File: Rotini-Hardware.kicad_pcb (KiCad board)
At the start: 4 copper layers, 62 x 21.6 mm, 116 parts, among them J1 Conn_01x02, J2 Conn_01x02, J200 SH_PPM, J201 SH_LED, J202 SH_LED, J60 Conn_Coaxial, Q20 AO3401A, Q30 LBSS84LT1G, Q31 2N7002, Q32 LBSS84LT1G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

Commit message: Hardware bought of Rotini V2
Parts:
- removed C50, C51: 100nF, Capacitor_SMD:C_0402_1005Metric
- removed C52: 10uF, Capacitor_SMD:C_0402_1005Metric
- removed J1, J2: Conn_01x02, Connector_PinHeader_2.54mm:PinHeader_1x02_P2.54mm_Vertical
- removed J200: SH_PPM, Connector_JST:JST_SH_SM04B-SRSS-TB_1x04-1MP_P1.00mm_Horizontal
- removed Q50, Q51: SS8050, Package_TO_SOT_SMD:SOT-23
- removed R10, R6, R7, R8, R9: 300R, Resistor_SMD:R_1206_3216Metric
- removed R2: 500R, Resistor_SMD:R_0402_1005Metric
- removed R50, R51, R52, R53: 1K, Resistor_SMD:R_0402_1005Metric
- removed R54, R55: 5.1K, Resistor_SMD:R_0402_1005Metric
- removed U50: CP2102-GMR, Package_DFN_QFN:QFN-28-1EP_5x5mm_P0.5mm_EP3.35x3.35mm
- removed U51: USB_C_Receptacle, AlfredoFootprints:USB_TYPE-C-31-M-12
- added ?: , , F.Cu at (8.50, 8.00)
- added ?: , , F.Cu at (-8.50, 8.00)
- added J203: SH_PPM, Connector_JST:JST_SH_SM03B-SRSS-TB_1x03-1MP_P1.00mm_Horizontal, F.Cu at (20.2, -4.70)
- added J205: VIN, AlfredoFootprints:TGD-antenna-THT, B.Cu at (-20.2, 8.50)
- added J206: GND, AlfredoFootprints:TGD-antenna-THT, B.Cu at (-20.2, 4.60)
- added J207: FOO, AlfredoFootprints:TGD-antenna-THT, B.Cu at (20.2, -2.25)
- added J208: BAR, AlfredoFootprints:TGD-antenna-THT, B.Cu at (20.2, -7.15)
- added J61: Conn_01x01_Female, AlfredoFootprints:TGD-antenna-THT, B.Cu at (-11.2, -8.30)
- added TP1: ELRS_TX, AlfredoFootprints:PogoPad1, B.Cu at (1.00, 4.00)
- added TP2: ELRS_RX, AlfredoFootprints:PogoPad1, B.Cu at (-1.50, 4.00)
- added TP3: ELRS_TX, AlfredoFootprints:PogoPad1, B.Cu at (-4.00, 4.00)
- J202: value SH_LED -> SH_POW; footprint Connector_JST:JST_SH_SM04B-SRSS-TB_1x04-1MP_P1.00mm_Horizontal -> Connector_JST:JST_SH_SM02B-SRSS-TB_1x02-1MP_P1.00mm_Horizontal
- JP1, JP2, JP60: moved to B.Cu
- R4: value 7K -> 3.3K
- R60: value 1K -> 12K
- moved D60 36.5 mm to (20.6, -9.50), turned to 180 degrees
- moved D20 32.9 mm to (15.2, 0.45), turned to 0 degrees
- moved R68 18.4 mm to (12.5, -0.95), turned to -90 degrees
- moved R56 18.3 mm to (22.9, 6.90), turned to 90 degrees
- moved R57 18.2 mm to (22.9, 4.90), turned to -90 degrees
- moved C102 17.3 mm to (-6.50, -8.40), turned to 0 degrees
- moved C103 16.9 mm to (-6.80, -9.40)
- moved J60 16.6 mm to (-11.4, -8.30), turned to 180 degrees
- moved C104 16.3 mm to (-6.00, -6.90), turned to 90 degrees
- moved JP2 15.8 mm to (4.70, 1.60), turned to 90 degrees
- moved L102 15.2 mm to (-7.00, -6.90), turned to 90 degrees
- moved R31 15.2 mm to (-15.5, -10.2), turned to 0 degrees
- moved JP1 13.7 mm to (9.70, 1.60), turned to -90 degrees
- moved R30 13.0 mm to (-17.3, -10.2), turned to 0 degrees
- moved L101 12.7 mm to (-8.50, -6.40), turned to 0 degrees
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- renumbered J201 to J204, R36 to R35
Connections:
- J202 pad 2: GND -> Net-(J202-Pad2)
- Q20 pad 3: Net-(J202-Pad3) -> Net-(J202-Pad2)
- R4 pad 1: Net-(R4-Pad1) -> SNS_VER
- R5 pad 2: Net-(R4-Pad1) -> SNS_VER
- U1 pad 10: unconnected-(U1-Pad10) -> SNS_VER
- U1 pad 28: Net-(R4-Pad1) -> unconnected-(U1-Pad28)
- U1 pad 48: Net-(R2-Pad2) -> unconnected-(U1-Pad48)
- U1 pad 49: E_RXD -> unconnected-(U1-Pad49)
- U60 pad 2: unconnected-(U60-Pad2) -> /ExpressLRS-RX/trace_antenna
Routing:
- net VBUS: track 78.5 -> 8.43 mm, vias 6 -> 0
- net VCC: track 26.3 -> 79.0 mm, vias 3 -> 4
- net Net-(D60-Pad2): track 1.07 -> 29.2 mm, vias 0 -> 2
- net E_RXD: track 27.5 -> 0.00 mm, vias 2 -> 0
- net E_TXD: track 27.4 -> 0.00 mm, vias 1 -> 0
- net SNS_VER: track 0.00 -> 25.8 mm, vias 0 -> 2
- net E_IO0: track 22.6 -> 5.33 mm, vias 2 -> 1
- net CP_RTS: track 16.8 -> 0.00 mm, vias 2 -> 0
- net /ExpressLRS-RX/trace_antenna: track 0.00 -> 16.5 mm, vias 0 -> 1
- net CP_DTR: track 16.3 -> 0.00 mm, vias 2 -> 0
- net LED_1: track 23.7 -> 38.2 mm
- net P_MISO: track 21.8 -> 35.4 mm
- net LED_2: track 22.8 -> 36.4 mm
- net E_EN: track 20.6 -> 7.79 mm, vias 2 -> 1
- net P_MOSI: track 15.5 -> 27.6 mm
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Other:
- board size 62 x 21.6 mm -> 47 x 21.6 mm
- board text added: "3V3"
- board text added: "ANT"
- board text added: "Alfredo Systems © 2022 Rotini V2"
- board text added: "BAR"
- board text added: "CS2"
- board text added: "FOO"
- board text added: "G"
- board text added: "GND"
- board text added: "MISO"
- board text added: "MOSI"
- board text added: "RX"
- board text added: "Rotini V2"
- board text added: "SCK"
- board text added: "TX"
- board text added: "V2"
- board text added: "VIN"
- board text added: "X"
- board text removed: "Rotini V1"
- board text removed: "V1"
- board text removed: "© 2022 Alfredo Systems"

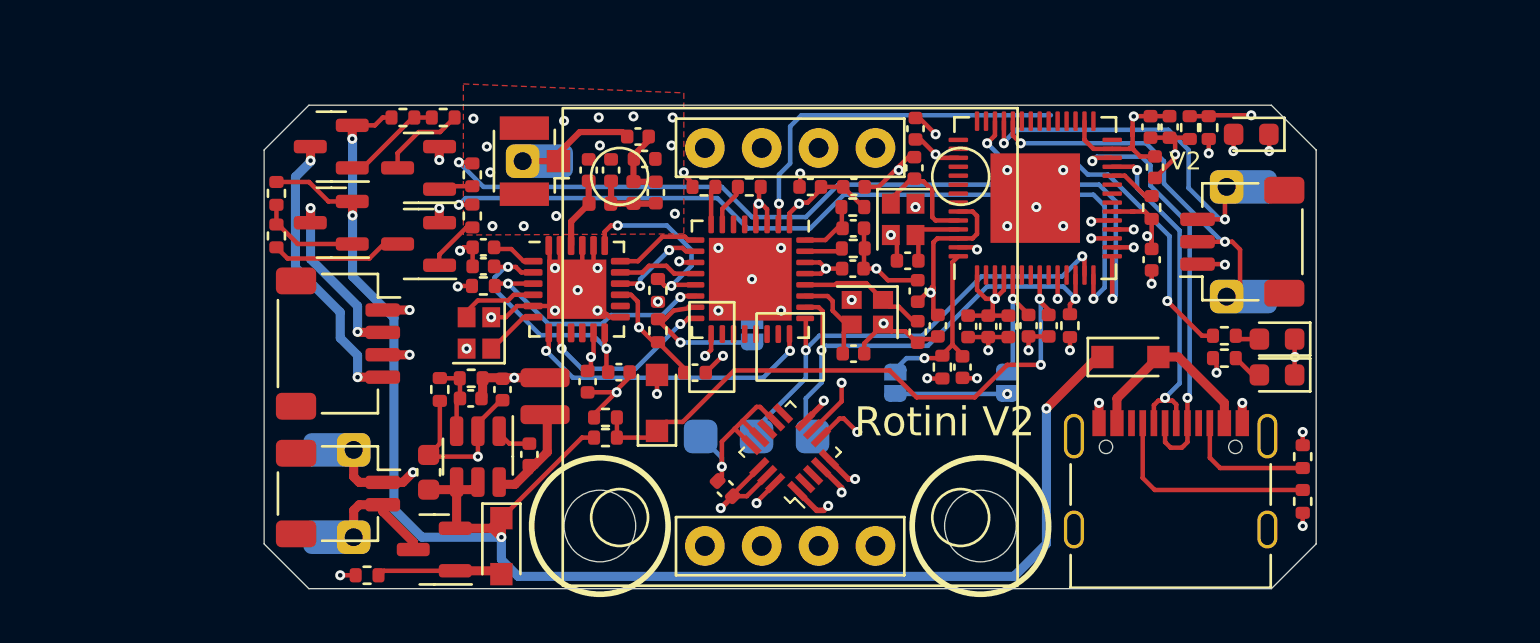
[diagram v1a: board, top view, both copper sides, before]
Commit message: Cleaned up schematic
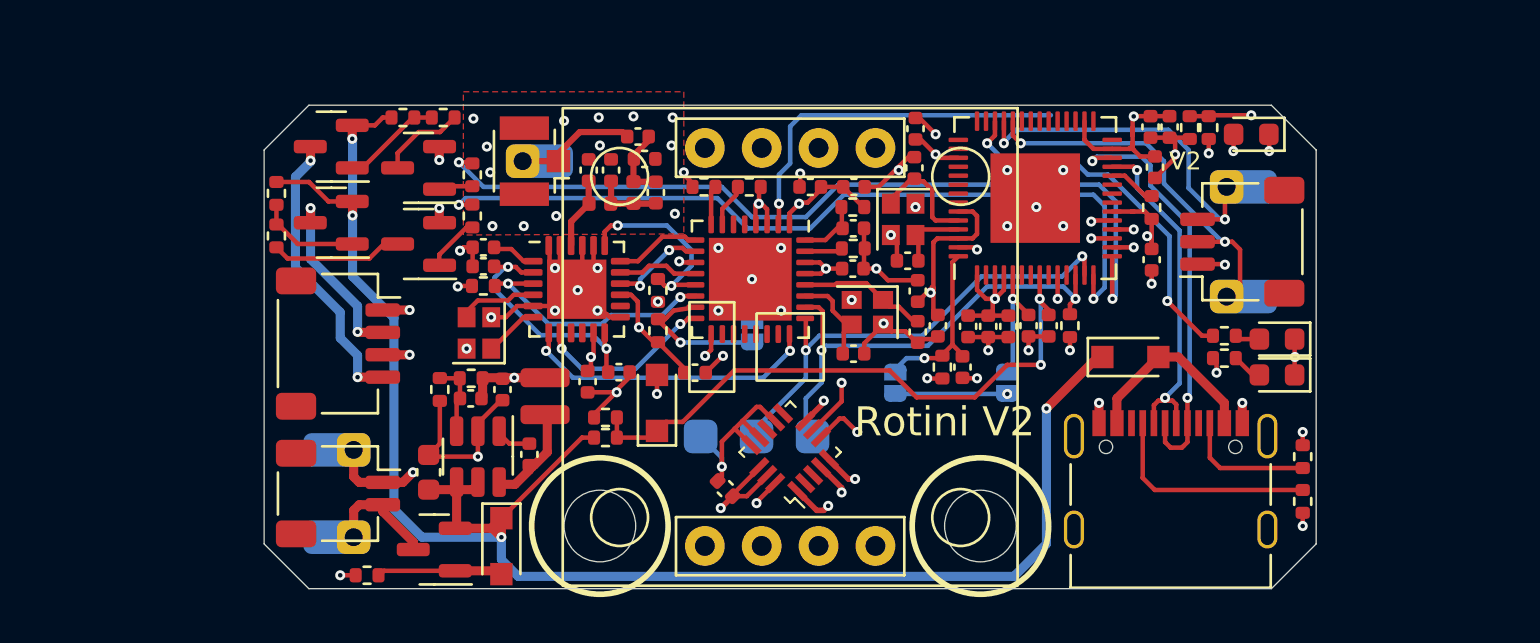
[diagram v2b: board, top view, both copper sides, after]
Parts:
- TP3: value ELRS_TX -> ELRS_GND
- turned R56 to -90 degrees
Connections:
- net VBUS renamed Net-(U52-PadA4)
- R56 pad 1: GND -> Net-(R56-Pad1)
- R56 pad 2: Net-(R56-Pad2) -> GND
- U52 pad A5: Net-(R56-Pad2) -> Net-(R56-Pad1)
- U60 pad 18: GPIO9 -> unconnected-(U60-Pad18)
- U60 pad 19: GPIO10 -> unconnected-(U60-Pad19)
- U60 pad 20: SD_CMD -> unconnected-(U60-Pad20)
- U60 pad 21: SD_CLK -> unconnected-(U60-Pad21)
- U60 pad 22: SD_D0 -> unconnected-(U60-Pad22)
- U60 pad 23: SD_D1 -> unconnected-(U60-Pad23)
- U60 pad 6: ADC -> unconnected-(U60-Pad6)
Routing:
- net Net-(R56-Pad2): track 9.82 -> 0.00 mm
- net Net-(R56-Pad1): track 0.00 -> 9.82 mm
